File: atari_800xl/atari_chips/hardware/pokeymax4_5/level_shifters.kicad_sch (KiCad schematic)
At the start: 2 parts, among them U3 SN74CB3T16211DGVR, U5 SN74CB3T16211DGVR

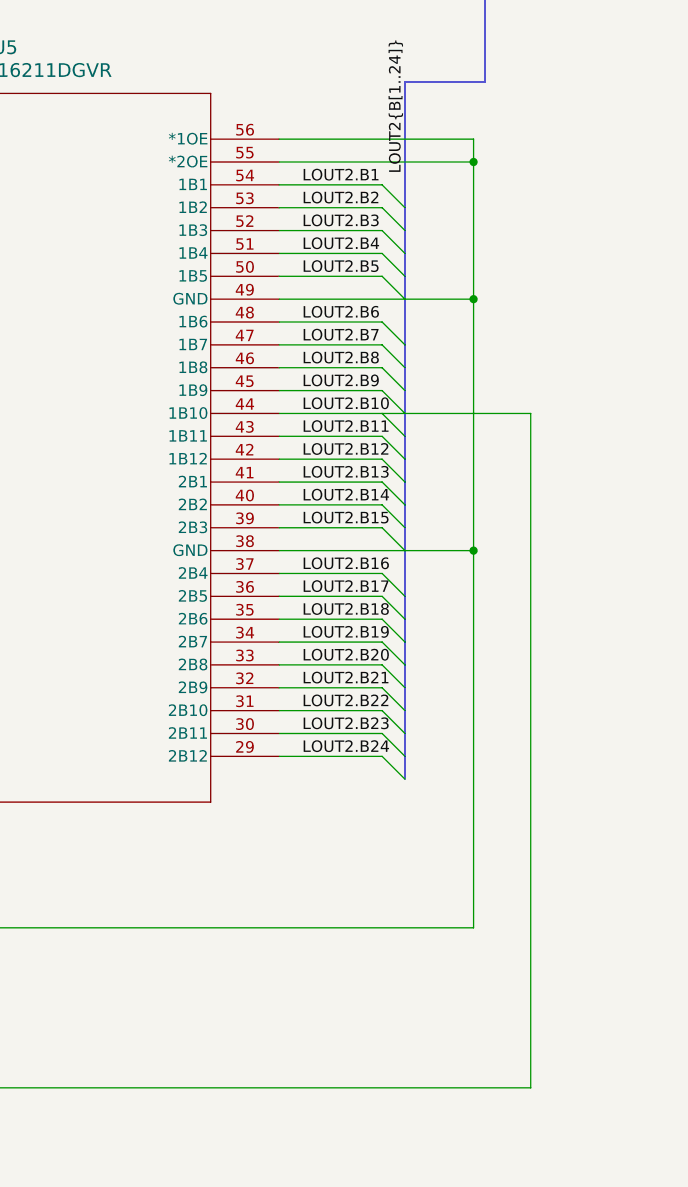
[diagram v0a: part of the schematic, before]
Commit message: Pokeymax v4_53 as produced
git-svn-id: svn+ssh://192.168.0.3/home/svnfpga/repo/trunk@1512 d6161ac3-aae1-4d52-9b05-ea9ac36b53d3
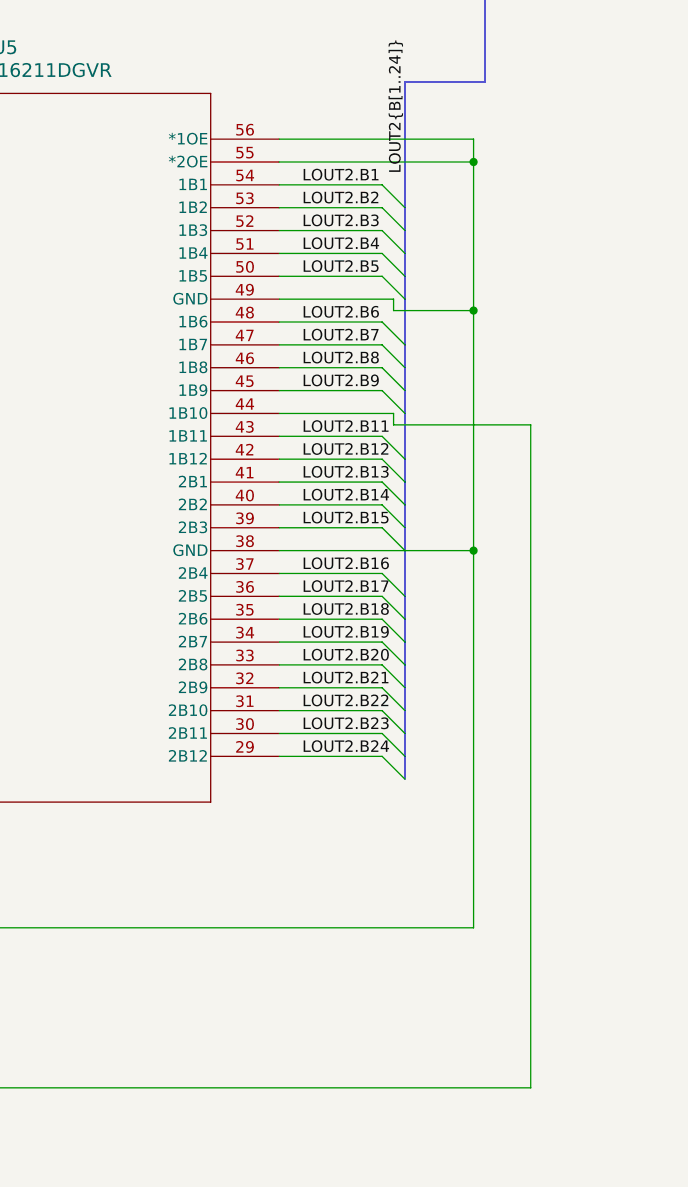
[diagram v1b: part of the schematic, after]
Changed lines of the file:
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@@
 	)
 	(junction
-		(at 151.13 102.87)
+		(at 266.7 76.2)
 		(diameter 0)
 		(color 0 0 0 0)
 	)
 	(junction
-		(at 266.7 74.93)
+		(at 151.13 102.87)
 		(diameter 0)
 		(color 0 0 0 0)
@@
 	)
 	(bus_entry
-		(at 256.54 87.63)
-		(size 2.54 2.54)
-		(stroke
-			(width 0)
-			(type default)
-		)
-	)
-	(bus_entry
 		(at 45.72 123.19)
 		(size 2.54 2.54)
@@
 	(wire
 		(pts
+			(xy 257.81 88.9) (xy 273.05 88.9)
+		)
+		(stroke
+			(width 0)
+			(type default)
+		)
+	)
+	(wire
+		(pts
 			(xy 173.99 123.19) (xy 184.15 123.19)
 		)
@@
 	(wire
 		(pts
+			(xy 266.7 76.2) (xy 266.7 102.87)
+		)
+		(stroke
+			(width 0)
+			(type default)
+		)
+	)
+	(wire
+		(pts
 			(xy 245.11 107.95) (xy 256.54 107.95)
 		)
@@
 	(wire
 		(pts
-			(xy 259.08 87.63) (xy 256.54 87.63)
+			(xy 257.81 74.93) (xy 257.81 76.2)
 		)
 		(stroke
@@
 	(wire
 		(pts
-			(xy 245.11 87.63) (xy 256.54 87.63)
+			(xy 245.11 87.63) (xy 257.81 87.63)
 		)
 		(stroke
@@
 		)
 	)
-	(wire
-		(pts
-			(xy 266.7 74.93) (xy 266.7 102.87)
-		)
-		(stroke
-			(width 0)
-			(type default)
-		)
-	)
 	(bus
 		(pts
@@
 	(wire
 		(pts
+			(xy 257.81 76.2) (xy 266.7 76.2)
+		)
+		(stroke
+			(width 0)
+			(type default)
+		)
+	)
+	(wire
+		(pts
 			(xy 119.38 118.11) (xy 130.81 118.11)
 		)
@@
 		)
 	)
+	(wire
+		(pts
+			(xy 257.81 87.63) (xy 257.81 88.9)
+		)
+		(stroke
+			(width 0)
+			(type default)
+		)
+	)
 	(bus
 		(pts
@@
 	(bus
 		(pts
-			(xy 259.08 87.63) (xy 259.08 90.17)
+			(xy 259.08 87.63) (xy 259.08 92.71)
 		)
 		(stroke
@@
 	(wire
 		(pts
-			(xy 266.7 59.69) (xy 266.7 74.93)
+			(xy 266.7 59.69) (xy 266.7 76.2)
 		)
 		(stroke
@@
 	(wire
 		(pts
-			(xy 245.11 74.93) (xy 259.08 74.93)
+			(xy 245.11 74.93) (xy 257.81 74.93)
 		)
 		(stroke
@@
 	(wire
 		(pts
-			(xy 259.08 74.93) (xy 266.7 74.93)
-		)
-		(stroke
-			(width 0)
-			(type default)
-		)
-	)
-	(wire
-		(pts
 			(xy 119.38 92.71) (xy 130.81 92.71)
 		)
@@
 		)
 	)
-	(bus
-		(pts
-			(xy 259.08 90.17) (xy 259.08 92.71)
-		)
-		(stroke
-			(width 0)
-			(type default)
-		)
-	)
 	(wire
 		(pts
@@
 	(wire
 		(pts
-			(xy 273.05 87.63) (xy 259.08 87.63)
-		)
-		(stroke
-			(width 0)
-			(type default)
-		)
-	)
-	(wire
-		(pts
 			(xy 35.56 74.93) (xy 35.56 102.87)
 		)
@@
 	(wire
 		(pts
-			(xy 273.05 162.56) (xy 273.05 87.63)
+			(xy 273.05 162.56) (xy 273.05 88.9)
 		)
 		(stroke
@@
 		(effects
 			(font
-				(size 1.27 1.27)
-			)
-			(justify left bottom)
-		)
-	)
-	(label "LOUT2.B10"
-		(at 247.65 87.63 0)
-		(effects
-			(font
